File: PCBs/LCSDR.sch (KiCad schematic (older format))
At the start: 5 parts, among them J12 Conn_01x01, J13 Conn_01x01, J14 Conn_01x01, J15 Conn_01x01, J6 I2C

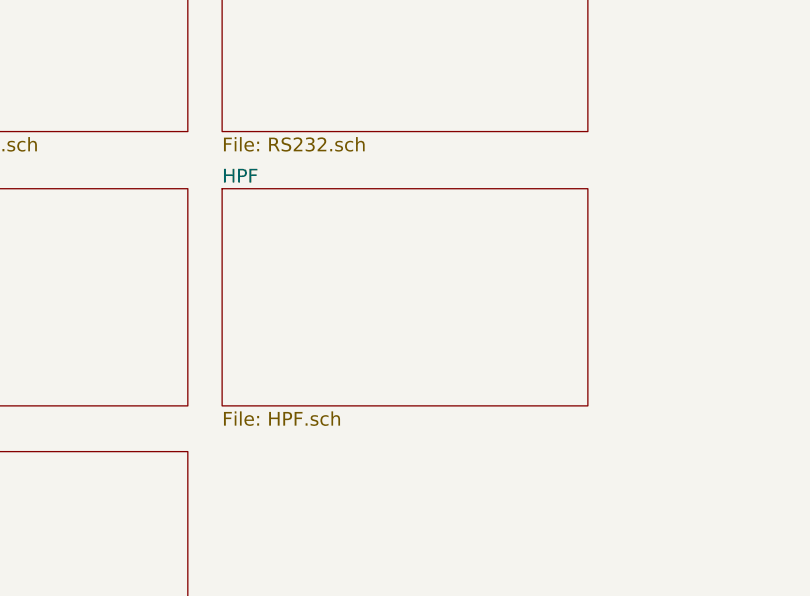
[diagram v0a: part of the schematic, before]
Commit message: ADX988 CAT: add FE, FI commands
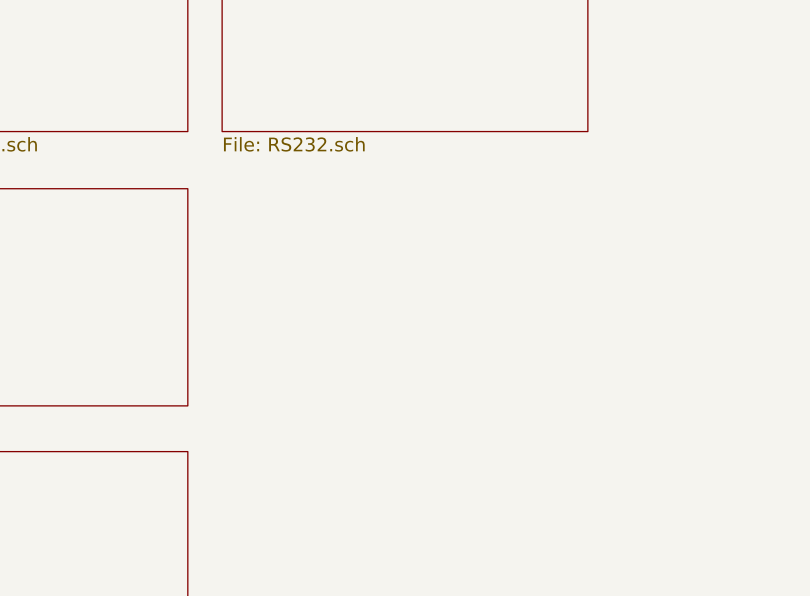
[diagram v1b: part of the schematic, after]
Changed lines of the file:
@@
 $Descr A4 11693 8268
 encoding utf-8
-Sheet 1 9
+Sheet 1 8
 Title "UT3MK VFO"
 Date "2016-02-18"
@@
 $EndComp
 $Comp
-L GND #PWR01
+L GND #PWR2
 U 1 1 5FFDFFFB
 P 8600 3200
-F 0 "#PWR01" H 8600 2950 50  0001 C CNN
+F 0 "#PWR2" H 8600 2950 50  0001 C CNN
 F 1 "GND" H 8600 3050 50  0001 C CNN
 F 2 "" H 8600 3200 50  0001 C CNN
@@
 $EndComp
 $Comp
-L +5V #PWR02
+L +5V #PWR1
 U 1 1 5FFE0CB0
 P 8450 3300
-F 0 "#PWR02" H 8450 3150 50  0001 C CNN
+F 0 "#PWR1" H 8450 3150 50  0001 C CNN
 F 1 "+5V" V 8450 3500 50  0000 C CNN
 F 2 "" H 8450 3300 50  0001 C CNN
@@
 $EndComp
 $Comp
-L GND #PWR03
+L GND #PWR3
 U 1 1 6000BED7
 P 8650 2600
-F 0 "#PWR03" H 8650 2350 50  0001 C CNN
+F 0 "#PWR3" H 8650 2350 50  0001 C CNN
 F 1 "GND" H 8650 2450 50  0001 C CNN
 F 2 "" H 8650 2600 50  0001 C CNN
@@
 F1 "RS232.sch" 60
 $EndSheet
-$Sheet
-S 4400 2200 1600 950
-U 630A35F6
-F0 "HPF" 60
-F1 "HPF.sch" 60
-$EndSheet
 $EndSCHEMATC

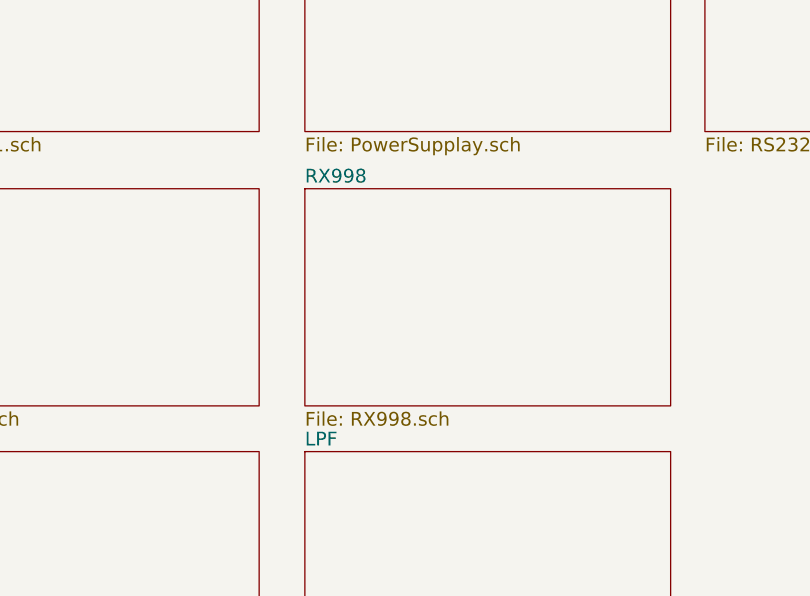
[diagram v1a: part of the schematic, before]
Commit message: discret, simple, CH340E
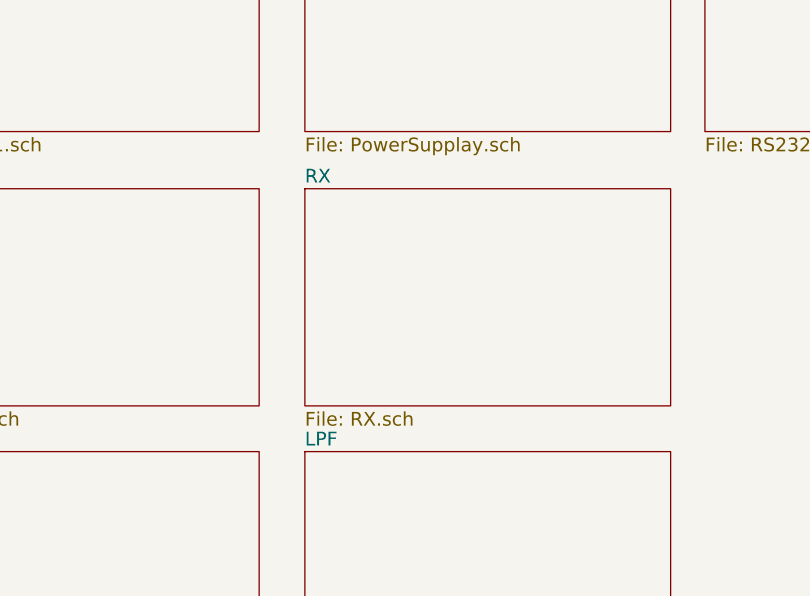
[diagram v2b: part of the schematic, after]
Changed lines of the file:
@@
 LIBS:BF998
 LIBS:relays
+LIBS:stm32
+LIBS:Interface_USB
+LIBS:Arduino
 LIBS:LCSDR-cache
 EELAYER 25 0
@@
 $EndComp
 $Comp
-L GND #PWR2
+L GND #PWR01
 U 1 1 5FFDFFFB
 P 8600 3200
-F 0 "#PWR2" H 8600 2950 50  0001 C CNN
+F 0 "#PWR01" H 8600 2950 50  0001 C CNN
 F 1 "GND" H 8600 3050 50  0001 C CNN
 F 2 "" H 8600 3200 50  0001 C CNN
@@
 $EndComp
 $Comp
-L +5V #PWR1
+L +5V #PWR02
 U 1 1 5FFE0CB0
 P 8450 3300
-F 0 "#PWR1" H 8450 3150 50  0001 C CNN
+F 0 "#PWR02" H 8450 3150 50  0001 C CNN
 F 1 "+5V" V 8450 3500 50  0000 C CNN
 F 2 "" H 8450 3300 50  0001 C CNN
@@
 $EndComp
 $Comp
-L GND #PWR3
+L GND #PWR03
 U 1 1 6000BED7
 P 8650 2600
-F 0 "#PWR3" H 8650 2350 50  0001 C CNN
+F 0 "#PWR03" H 8650 2350 50  0001 C CNN
 F 1 "GND" H 8650 2450 50  0001 C CNN
 F 2 "" H 8650 2600 50  0001 C CNN
@@
 S 2650 2200 1600 950
 U 63054DF3
-F0 "RX998" 60
-F1 "RX998.sch" 60
+F0 "RX" 60
+F1 "RX.sch" 60
 $EndSheet
 $Sheet

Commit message: INIT project, si5351 generate properly frequency
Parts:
- removed J6: I2C, Pin_Headers:Pin_Header_Straight_1x04_Pitch2.54mm, symbol Conn_01x04
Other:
- moved on the sheet: J12, J13, J14, J15
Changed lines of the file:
@@
 $Descr A4 11693 8268
 encoding utf-8
-Sheet 1 8
+Sheet 1 7
 Title "UT3MK VFO"
 Date "2016-02-18"
@@
 $EndDescr
 $Comp
-L Conn_01x04 J6
-U 1 1 5FFDFD88
-P 9000 3300
-F 0 "J6" H 9000 3500 50  0000 C CNN
-F 1 "I2C" H 9000 3000 50  0000 C CNN
-F 2 "Pin_Headers:Pin_Header_Straight_1x04_Pitch2.54mm" H 9000 3300 50  0001 C CNN
-F 3 "" H 9000 3300 50  0001 C CNN
-	1    9000 3300
-	1    0    0    -1
-$EndComp
-$Comp
-L GND #PWR01
-U 1 1 5FFDFFFB
-P 8600 3200
-F 0 "#PWR01" H 8600 2950 50  0001 C CNN
-F 1 "GND" H 8600 3050 50  0001 C CNN
-F 2 "" H 8600 3200 50  0001 C CNN
-F 3 "" H 8600 3200 50  0001 C CNN
-	1    8600 3200
-	0    1    1    0
-$EndComp
-$Comp
-L +5V #PWR02
-U 1 1 5FFE0CB0
-P 8450 3300
-F 0 "#PWR02" H 8450 3150 50  0001 C CNN
-F 1 "+5V" V 8450 3500 50  0000 C CNN
-F 2 "" H 8450 3300 50  0001 C CNN
-F 3 "" H 8450 3300 50  0001 C CNN
-	1    8450 3300
-	0    -1   -1   0
-$EndComp
-Wire Wire Line
-	8600 3200 8800 3200
-Text GLabel 8700 3400 0    60   BiDi ~ 0
-SDA
-Wire Wire Line
-	8450 3300 8800 3300
-Text GLabel 8700 3600 0    60   Output ~ 0
-SCL
-Wire Wire Line
-	8700 3400 8800 3400
-Wire Wire Line
-	8700 3600 8750 3600
-Wire Wire Line
-	8750 3600 8750 3500
-Wire Wire Line
-	8750 3500 8800 3500
-$Comp
 L Conn_01x01 J12
 U 1 1 6000B737
-P 9050 1550
-F 0 "J12" H 9050 1650 50  0000 C CNN
-F 1 "Conn_01x01" H 9050 1450 50  0000 C CNN
-F 2 "Mounting_Holes:MountingHole_3.2mm_M3_DIN965_Pad" H 9050 1550 50  0001 C CNN
-F 3 "" H 9050 1550 50  0001 C CNN
-	1    9050 1550
+P 7200 1250
+F 0 "J12" H 7200 1350 50  0000 C CNN
+F 1 "Conn_01x01" H 7200 1150 50  0000 C CNN
+F 2 "Mounting_Holes:MountingHole_3.2mm_M3_DIN965_Pad" H 7200 1250 50  0001 C CNN
+F 3 "" H 7200 1250 50  0001 C CNN
+	1    7200 1250
 	1    0    0    -1
 $EndComp
@@
 L Conn_01x01 J13
 U 1 1 6000BA3A
-P 9050 1850
-F 0 "J13" H 9050 1950 50  0000 C CNN
-F 1 "Conn_01x01" H 9050 1750 50  0000 C CNN
-F 2 "Mounting_Holes:MountingHole_3.2mm_M3_DIN965_Pad" H 9050 1850 50  0001 C CNN
-F 3 "" H 9050 1850 50  0001 C CNN
-	1    9050 1850
+P 7200 1550
+F 0 "J13" H 7200 1650 50  0000 C CNN
+F 1 "Conn_01x01" H 7200 1450 50  0000 C CNN
+F 2 "Mounting_Holes:MountingHole_3.2mm_M3_DIN965_Pad" H 7200 1550 50  0001 C CNN
+F 3 "" H 7200 1550 50  0001 C CNN
+	1    7200 1550
 	1    0    0    -1
 $EndComp
@@
 L Conn_01x01 J14
 U 1 1 6000BB7C
-P 9050 2150
-F 0 "J14" H 9050 2250 50  0000 C CNN
-F 1 "Conn_01x01" H 9050 2050 50  0000 C CNN
-F 2 "Mounting_Holes:MountingHole_3.2mm_M3_DIN965_Pad" H 9050 2150 50  0001 C CNN
-F 3 "" H 9050 2150 50  0001 C CNN
-	1    9050 2150
+P 7200 1850
+F 0 "J14" H 7200 1950 50  0000 C CNN
+F 1 "Conn_01x01" H 7200 1750 50  0000 C CNN
+F 2 "Mounting_Holes:MountingHole_3.2mm_M3_DIN965_Pad" H 7200 1850 50  0001 C CNN
+F 3 "" H 7200 1850 50  0001 C CNN
+	1    7200 1850
 	1    0    0    -1
 $EndComp
@@
 L Conn_01x01 J15
 U 1 1 6000BCC1
-P 9050 2450
-F 0 "J15" H 9050 2550 50  0000 C CNN
-F 1 "Conn_01x01" H 9050 2350 50  0000 C CNN
-F 2 "Mounting_Holes:MountingHole_3.2mm_M3_DIN965_Pad" H 9050 2450 50  0001 C CNN
-F 3 "" H 9050 2450 50  0001 C CNN
-	1    9050 2450
+P 7200 2150
+F 0 "J15" H 7200 2250 50  0000 C CNN
+F 1 "Conn_01x01" H 7200 2050 50  0000 C CNN
+F 2 "Mounting_Holes:MountingHole_3.2mm_M3_DIN965_Pad" H 7200 2150 50  0001 C CNN
+F 3 "" H 7200 2150 50  0001 C CNN
+	1    7200 2150
 	1    0    0    -1
 $EndComp
 $Comp
-L GND #PWR03
+L GND #PWR01
 U 1 1 6000BED7
-P 8650 2600
-F 0 "#PWR03" H 8650 2350 50  0001 C CNN
-F 1 "GND" H 8650 2450 50  0001 C CNN
-F 2 "" H 8650 2600 50  0001 C CNN
-F 3 "" H 8650 2600 50  0001 C CNN
-	1    8650 2600
+P 6800 2300
+F 0 "#PWR01" H 6800 2050 50  0001 C CNN
+F 1 "GND" H 6800 2150 50  0001 C CNN
+F 2 "" H 6800 2300 50  0001 C CNN
+F 3 "" H 6800 2300 50  0001 C CNN
+	1    6800 2300
 	1    0    0    -1
 $EndComp
 Wire Wire Line
-	8650 1550 8650 2600
+	6800 1250 6800 2300
 Wire Wire Line
-	8650 1550 8850 1550
+	6800 1250 7000 1250
 Wire Wire Line
-	8850 1850 8650 1850
-Connection ~ 8650 1850
+	7000 1550 6800 1550
+Connection ~ 6800 1550
 Wire Wire Line
-	8850 2150 8650 2150
-Connection ~ 8650 2150
+	7000 1850 6800 1850
+Connection ~ 6800 1850
 Wire Wire Line
-	8850 2450 8650 2450
-Connection ~ 8650 2450
+	7000 2150 6800 2150
+Connection ~ 6800 2150
 $Sheet
 S 850  1000 1600 950
@@
 F1 "LPF.sch" 60
 $EndSheet
-$Sheet
-S 4400 1000 1600 950
-U 6307088C
-F0 "RS232" 60
-F1 "RS232.sch" 60
-$EndSheet
 $EndSCHEMATC
